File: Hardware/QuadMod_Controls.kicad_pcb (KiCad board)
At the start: 2 copper layers, 70.6 x 111.5 mm, 24 parts, among them J1 Conn_01x08_Pin, J10 Audio_Out_L, J11 Audio_Out_R, J13 Audio_In, J2 Conn_01x08_Pin, J3 Conn_01x08_Pin, J4 Conn_01x08_Pin, J5 AudioJack2_Ground_Switch, J6 AudioJack2_Ground_Switch, J7 AudioJack2_Ground_Switch, J8 AudioJack2_Ground_Switch, J9 AudioJack2_Ground_Switch, SW1 FX_Type_Switch

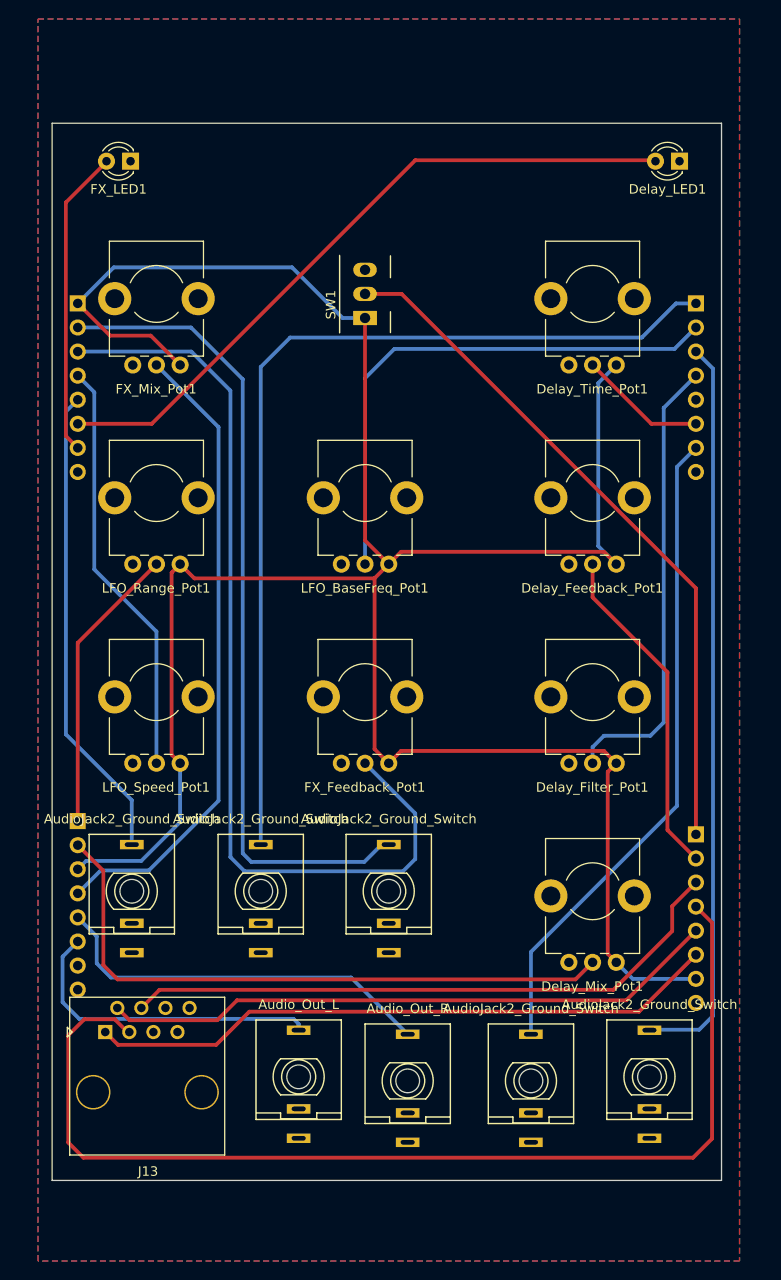
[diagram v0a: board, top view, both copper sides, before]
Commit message: Started adding additional clock LED
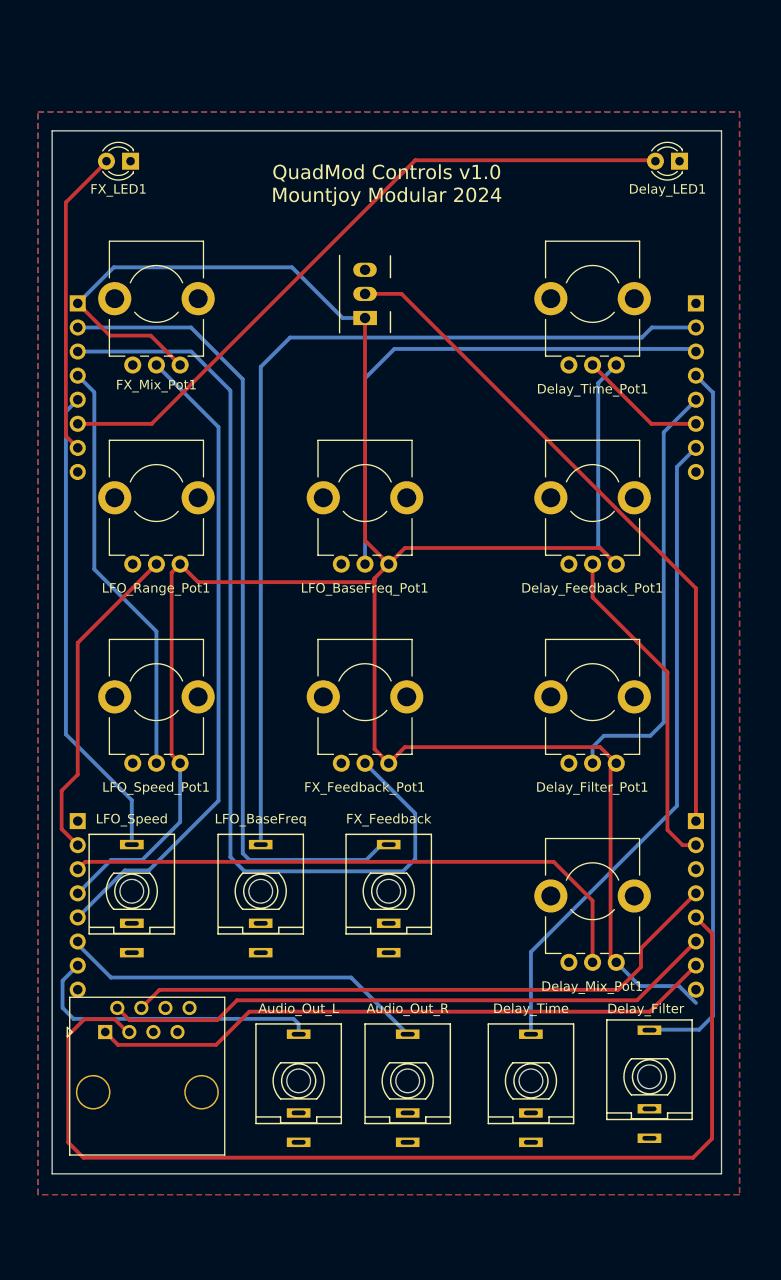
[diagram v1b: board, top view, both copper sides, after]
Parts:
- J5: value AudioJack2_Ground_Switch -> Delay_Time
- J6: value AudioJack2_Ground_Switch -> Delay_Filter
- J7: value AudioJack2_Ground_Switch -> LFO_BaseFreq
- J8: value AudioJack2_Ground_Switch -> FX_Feedback
- J9: value AudioJack2_Ground_Switch -> LFO_Speed
- moved J3 1.40 mm to (167.9, 123.6)
- moved J10 0.43 mm to (126.0, 151.0)
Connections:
- J1 pad 1: /LFO_BASEFREQ_CV -> GND
- J1 pad 2: /LFO_BASEFREQ_POT -> /LFO_BASEFREQ_CV
- J1 pad 3: /DLY_FILTER_CV -> /LFO_BASEFREQ_POT
- J1 pad 4: /DLY_FILTER_POT -> /DLY_FILTER_CV
- J1 pad 5: GND -> /DLY_FILTER_POT
- J3 pad 3: /IN4 -> GND
- J3 pad 4: /IN3 -> /IN4
- J3 pad 5: /IN2 -> /IN3
- J3 pad 6: /IN1 -> /IN2
- J3 pad 7: +3.3VA -> /IN1
- J3 pad 8: GND -> +3.3VA
- J4 pad 1: /LFO_RANGE -> GND
- J4 pad 2: /DLY_MIX -> /LFO_RANGE
- J4 pad 3: +3.3VA -> /DLY_MIX
- J4 pad 4: /FX_MIX -> +3.3VA
- J4 pad 5: /OUT_AMP2 -> /FX_MIX
- J4 pad 6: /OUT_AMP1 -> /OUT_AMP2
- J4 pad 7: GND -> /OUT_AMP1
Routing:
- net /LFO_RANGE: track 30.5 -> 34.5 mm
- net /DLY_MIX: track 66.7 -> 62.8 mm
- net +3.3VA: track 262.3 -> 265.4 mm
- net /OUT_AMP2: track 41.6 -> 39.0 mm
- net /DLY_FILTER_POT: track 48.3 -> 45.7 mm
- net /DLY_FILTER_CV: track 78.1 -> 75.6 mm
- net /OUT_AMP1: track 33.6 -> 31.4 mm
- net /FX_TYPE: track 73.7 -> 72.3 mm
- net /IN3: track 113.6 -> 112.4 mm
- net /LFO_BASEFREQ_CV: track 99.1 -> 98.0 mm
- net /FX_MIX: track 67.6 -> 68.6 mm
- net /IN4: track 65.5 -> 64.7 mm
- net /LFO_BASEFREQ_POT: track 56.7 -> 55.9 mm
- net /DLY_FEEDBACK: track 35.6 -> 35.0 mm
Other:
- board size 70.6 x 111.5 mm -> 70.6 x 110 mm

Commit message: Clean up of schematics and PCBS
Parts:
- Delay_LED1: value LED -> LED_Dual_AKA; footprint Custom_Footprints:LED_D3.0mm -> Custom_Footprints:LED_D3.0mm-3
- SW1: footprint Custom_Footprints:SPDTSubMiniature -> Custom_Footprints:SPDT_Miniature
- moved SW1 2.54 mm to (133.0, 68.0)
- moved J6 0.43 mm to (163.0, 151.0)
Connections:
- Delay_LED1 pad 1: GND -> /CLOCKED_LED
- Delay_LED1 pad 2: /DELAY_LED -> GND
- J2 pad 1: +3.3VA -> GND
- J2 pad 6: /DELAY_LED -> /CLOCKED_LED
- J2 pad 7: /FX_LED -> /DELAY_LED
- J2 pad 8: GND -> /FX_LED
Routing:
- net /CLOCKED_LED: track 0.00 -> 80.4 mm
- net +3.3VA: track 265.4 -> 235.8 mm
- net /DELAY_LED: track 72.5 -> 76.4 mm
- net /FX_LED: track 32.5 -> 35.1 mm
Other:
- board text added: "FX Type"
- board text added: "J1"
- board text added: "J2"
- board text added: "J3"
- board text added: "J4"

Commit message: Draft Gerber Creation
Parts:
- added PANEL: Panel, Custom_Footprints:3D_Dummy, F.Cu at (135.3, 105.3)
- added REF**: 3D_Dummy, Custom_Footprints:3D_Dummy, F.Cu at (135.3, 99.8)
- J1, J2, J3, J4: footprint Connector_PinHeader_2.54mm:PinHeader_1x08_P2.54mm_Vertical -> Connector_PinSocket_2.54mm:PinSocket_1x08_P2.54mm_Vertical
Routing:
- net /IN3: track 112.4 -> 106.6 mm
- net /LFO_BASEFREQ_CV: track 98.0 -> 99.0 mm
- net GND: vias 0 -> 77
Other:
- board size 70.6 x 110 mm -> 70.6 x 110.8 mm
